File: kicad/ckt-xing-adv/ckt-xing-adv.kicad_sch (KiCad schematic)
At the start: 130 parts, among them J1 Screw_Terminal_01x02, J10 SM04B-SRSS, J11 SM04B-SRSS, J12 SM04B-SRSS, J13 Conn_02x03_Row_Letter_First, J14 Conn_02x03_Row_Letter_First, J15 Conn_02x05_Counter_Clockwise, J16 SM04B-SRSS, J17 Screw_Terminal_01x02, J18 Screw_Terminal_01x02, J2 Screw_Terminal_01x02, J3 Screw_Terminal_01x02, J4 SM04B-SRSS, J5 SM04B-SRSS, J6 SM04B-SRSS, J7 SM04B-SRSS, J8 SM04B-SRSS, J9 SM04B-SRSS, Q1 ZXMS6004FF, Q2 ZXMS6004FF, Q3 ZXMS6004FF, SW1 FSM4JSMATR, SW2 FSM4JSMATR, SW3 FSM4JSMATR, U1 AP7381-33Y, U2 AP63205WU, U3 W25Q128JVS, U4 ATtiny861A-S, U5 PCA9685PW, U6 PCA9555D, U7 PAM8301, U8 DRV8231A, U9 DRV8231A

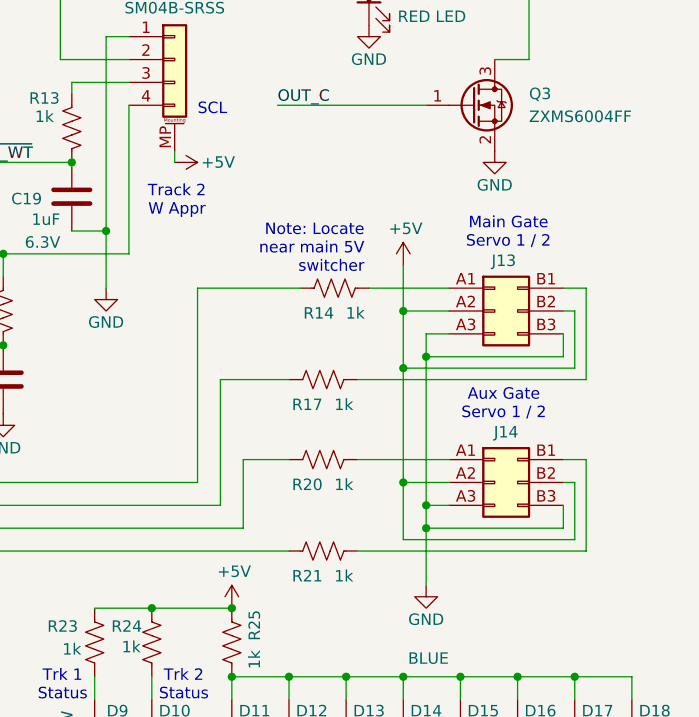
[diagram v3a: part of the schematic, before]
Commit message: Add test points for servo outputs Feedback from Michael on text position, etc
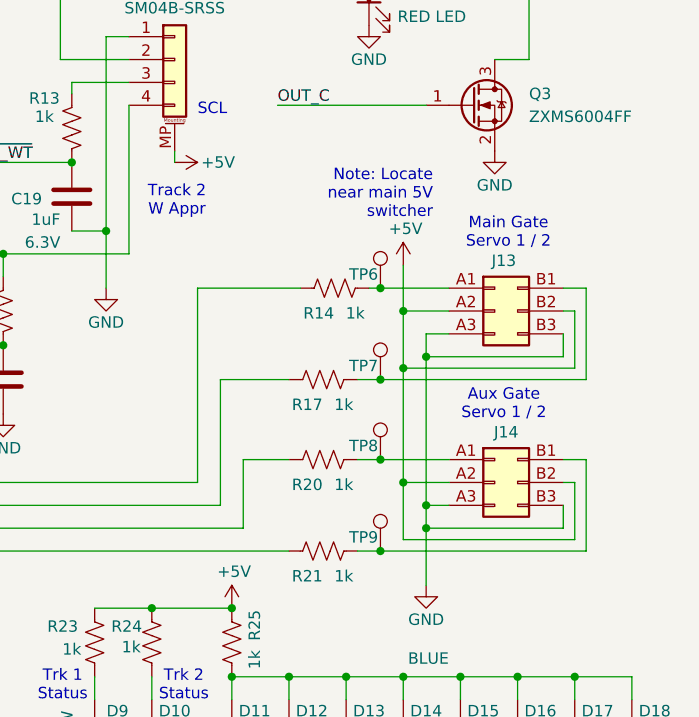
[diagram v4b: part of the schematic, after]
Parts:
- added TP6, TP7, TP8, TP9: TestPoint, TestPoint:TestPoint_Pad_D2.0mm, symbol Connector:TestPoint
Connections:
- net at J13.A1 (Pin_a1), R14.2: now also TP6.1
- net at J13.B1 (Pin_b1), R17.2: now also TP7.1
- net at J14.A1 (Pin_a1), R20.2: now also TP8.1
- net at J14.B1 (Pin_b1), R21.2: now also TP9.1

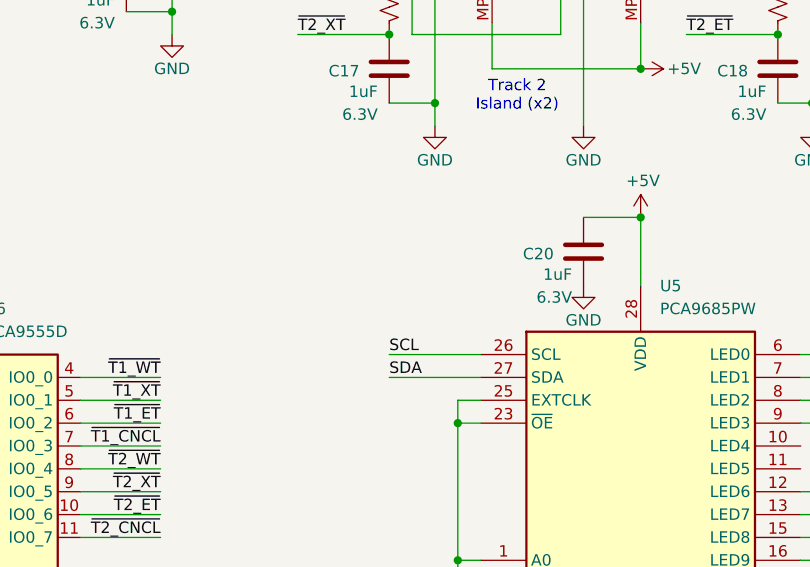
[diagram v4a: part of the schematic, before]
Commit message: Update to v1.1, adding level shifters between the CPU and the 9685, since it's in the 5V domain
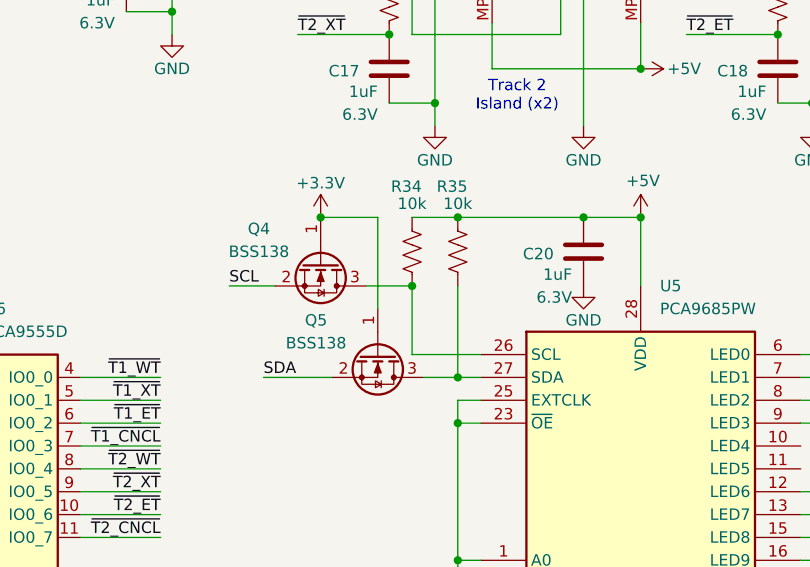
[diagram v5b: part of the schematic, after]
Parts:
- added Q4, Q5: BSS138, Package_TO_SOT_SMD:SOT-23, symbol Transistor_FET:BSS138
- added R34, R35: 10k, Resistor_SMD:R_0805_2012Metric, symbol Device:R_US
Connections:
- net +3.3V: now also Q4.1 (G), Q5.1 (G)
- net +5V: now also R34.2, R35.2
- net SCL: now also Q4.2 (S); no longer U5.26 (SCL)
- net SDA: now also Q5.2 (S); no longer U5.27 (SDA)
- new net: Q4.3 (D), R34.1, U5.26 (SCL)
- new net: Q5.3 (D), R35.1, U5.27 (SDA)

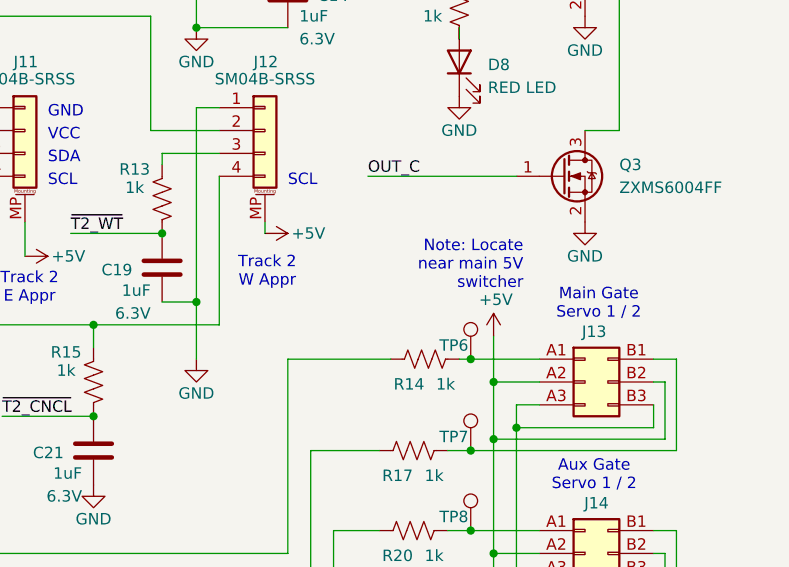
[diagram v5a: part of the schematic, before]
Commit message: Add electrolytic to servo drivers
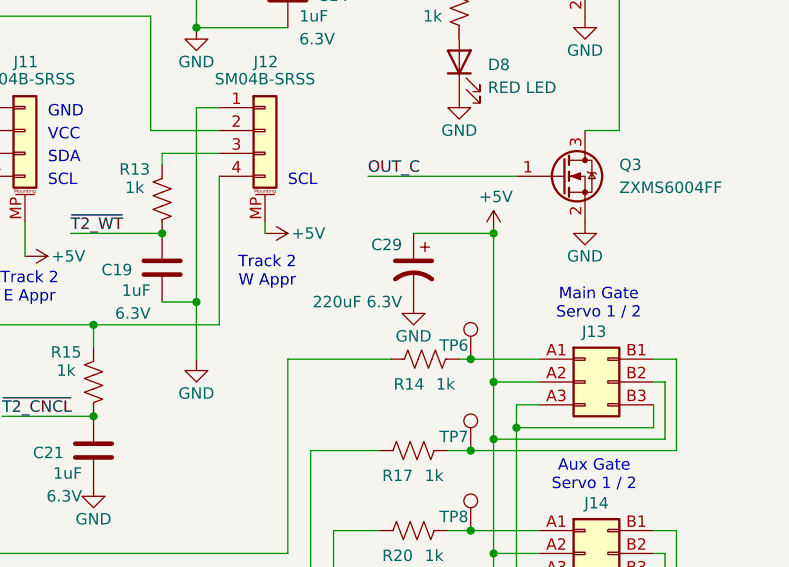
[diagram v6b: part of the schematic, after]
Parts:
- added C29: 220uF 6.3V, Capacitor_SMD:CP_Elec_6.3x5.8, symbol Device:C_Polarized_US
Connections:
- net +5V: now also C29.1
- net GND: now also C29.2
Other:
- note removed: "Note: Locate near main 5V switcher"
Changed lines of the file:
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@@
 		)
 	)
-	(text "Note: Locate\nnear main 5V\nswitcher"
-		(exclude_from_sim no)
-		(at 314.452 95.25 0)
-		(effects
-			(font
-				(size 1.27 1.27)
-			)
-			(justify right bottom)
-		)
-	)
 	(text "SCL"
 		(exclude_from_sim no)
@@
 	)
 	(junction
+		(at 311.15 88.9)
+		(diameter 0)
+		(color 0 0 0 0)
+	)
+	(junction
 		(at 129.54 129.54)
 		(diameter 0)
@@
 	(wire
 		(pts
-			(xy 311.15 100.33) (xy 311.15 105.41)
+			(xy 311.15 88.9) (xy 311.15 105.41)
 		)
 		(stroke
@@
 	(wire
 		(pts
+			(xy 302.26 88.9) (xy 311.15 88.9)
+		)
+		(stroke
+			(width 0)
+			(type default)
+		)
+	)
+	(wire
+		(pts
 			(xy 73.66 105.41) (xy 83.82 105.41)
 		)
@@
 	)
 	(symbol
+		(lib_id "Device:C_Polarized_US")
+		(at 302.26 92.71 0)
+		(mirror y)
+		(unit 1)
+		(exclude_from_sim no)
+		(in_bom yes)
+		(on_board yes)
+		(dnp no)
+		(property "Reference" "C29"
+			(at 300.99 90.17 0)
+			(effects
+				(font
+					(size 1.27 1.27)
+				)
+				(justify left)
+			)
+		)
+		(property "Value" "220uF 6.3V"
+			(at 300.99 96.52 0)
+			(effects
+				(font
+					(size 1.27 1.27)
+				)
+				(justify left)
+			)
+		)
+		(property "Footprint" "Capacitor_SMD:CP_Elec_6.3x5.8"
+			(at 302.26 92.71 0)
+			(effects
+				(font
+					(size 1.27 1.27)
+				)
+				(hide yes)
+			)
+		)
+		(property "Datasheet" "~"
+			(at 302.26 92.71 0)
+			(effects
+				(font
+					(size 1.27 1.27)
+				)
+				(hide yes)
+			)
+		)
+		(property "Description" ""
+			(at 302.26 92.71 0)
+			(effects
+				(font
+					(size 1.27 1.27)
+				)
+			)
+		)
+		(pin "1"
+		)
+		(pin "2"
+		)
+		(instances
+			(project "ckt-xing-adv"
+				(path "/ee2a1513-8489-42c3-8daf-9d032b383b2d"
+					(reference "C29")
+					(unit 1)
+				)
+			)
+		)
+	)
+	(symbol
 		(lib_id "Connector_Generic_MountingPin:Conn_01x04_MountingPin")
 		(at 215.9 35.56 0)
@@
 	)
 	(symbol
+		(lib_id "power:GND")
+		(at 302.26 96.52 0)
+		(mirror y)
+		(unit 1)
+		(exclude_from_sim no)
+		(in_bom yes)
+		(on_board yes)
+		(dnp no)
+		(property "Reference" "#PWR066"
+			(at 302.26 102.87 0)
+			(effects
+				(font
+					(size 1.27 1.27)
+				)
+				(hide yes)
+			)
+		)
+		(property "Value" "GND"
+			(at 302.26 100.33 0)
+			(effects
+				(font
+					(size 1.27 1.27)
+				)
+			)
+		)
+		(property "Footprint" ""
+			(at 302.26 96.52 0)
+			(effects
+				(font
+					(size 1.27 1.27)
+				)
+				(hide yes)
+			)
+		)
+		(property "Datasheet" ""
+			(at 302.26 96.52 0)
+			(effects
+				(font
+					(size 1.27 1.27)
+				)
+				(hide yes)
+			)
+		)
+		(property "Description" ""
+			(at 302.26 96.52 0)
+			(effects
+				(font
+					(size 1.27 1.27)
+				)
+			)
+		)
+		(pin "1"
+		)
+		(instances
+			(project "ckt-xing-adv"
+				(path "/ee2a1513-8489-42c3-8daf-9d032b383b2d"
+					(reference "#PWR066")
+					(unit 1)
+				)
+			)
+		)
+	)
+	(symbol
 		(lib_id "Connector_Generic_MountingPin:Conn_01x04_MountingPin")
 		(at 186.69 67.31 0)
@@
 	(symbol
 		(lib_id "power:+5V")
-		(at 311.15 100.33 0)
+		(at 311.15 88.9 0)
 		(unit 1)
 		(exclude_from_sim no)
@@
 		(dnp no)
 		(property "Reference" "#PWR028"
-			(at 311.15 104.14 0)
+			(at 311.15 92.71 0)
 			(effects
 				(font
@@
 		)
 		(property "Value" "+5V"
-			(at 311.404 96.266 0)
+			(at 311.404 84.836 0)
 			(effects
 				(font
@@
 		)
 		(property "Footprint" ""
-			(at 311.15 100.33 0)
+			(at 311.15 88.9 0)
 			(effects
 				(font
@@
 		)
 		(property "Datasheet" ""
-			(at 311.15 100.33 0)
+			(at 311.15 88.9 0)
 			(effects
 				(font
@@
 		)
 		(property "Description" ""
-			(at 311.15 100.33 0)
+			(at 311.15 88.9 0)
 			(effects
 				(font
